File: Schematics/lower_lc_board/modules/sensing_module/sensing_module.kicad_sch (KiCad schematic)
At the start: 26 parts, among them J4 HALL-1, J5 HALL-2, Q3 2N7002, U11 SI2301CDS-T1-GE3, U9 ADC_ADS131M04IPWR

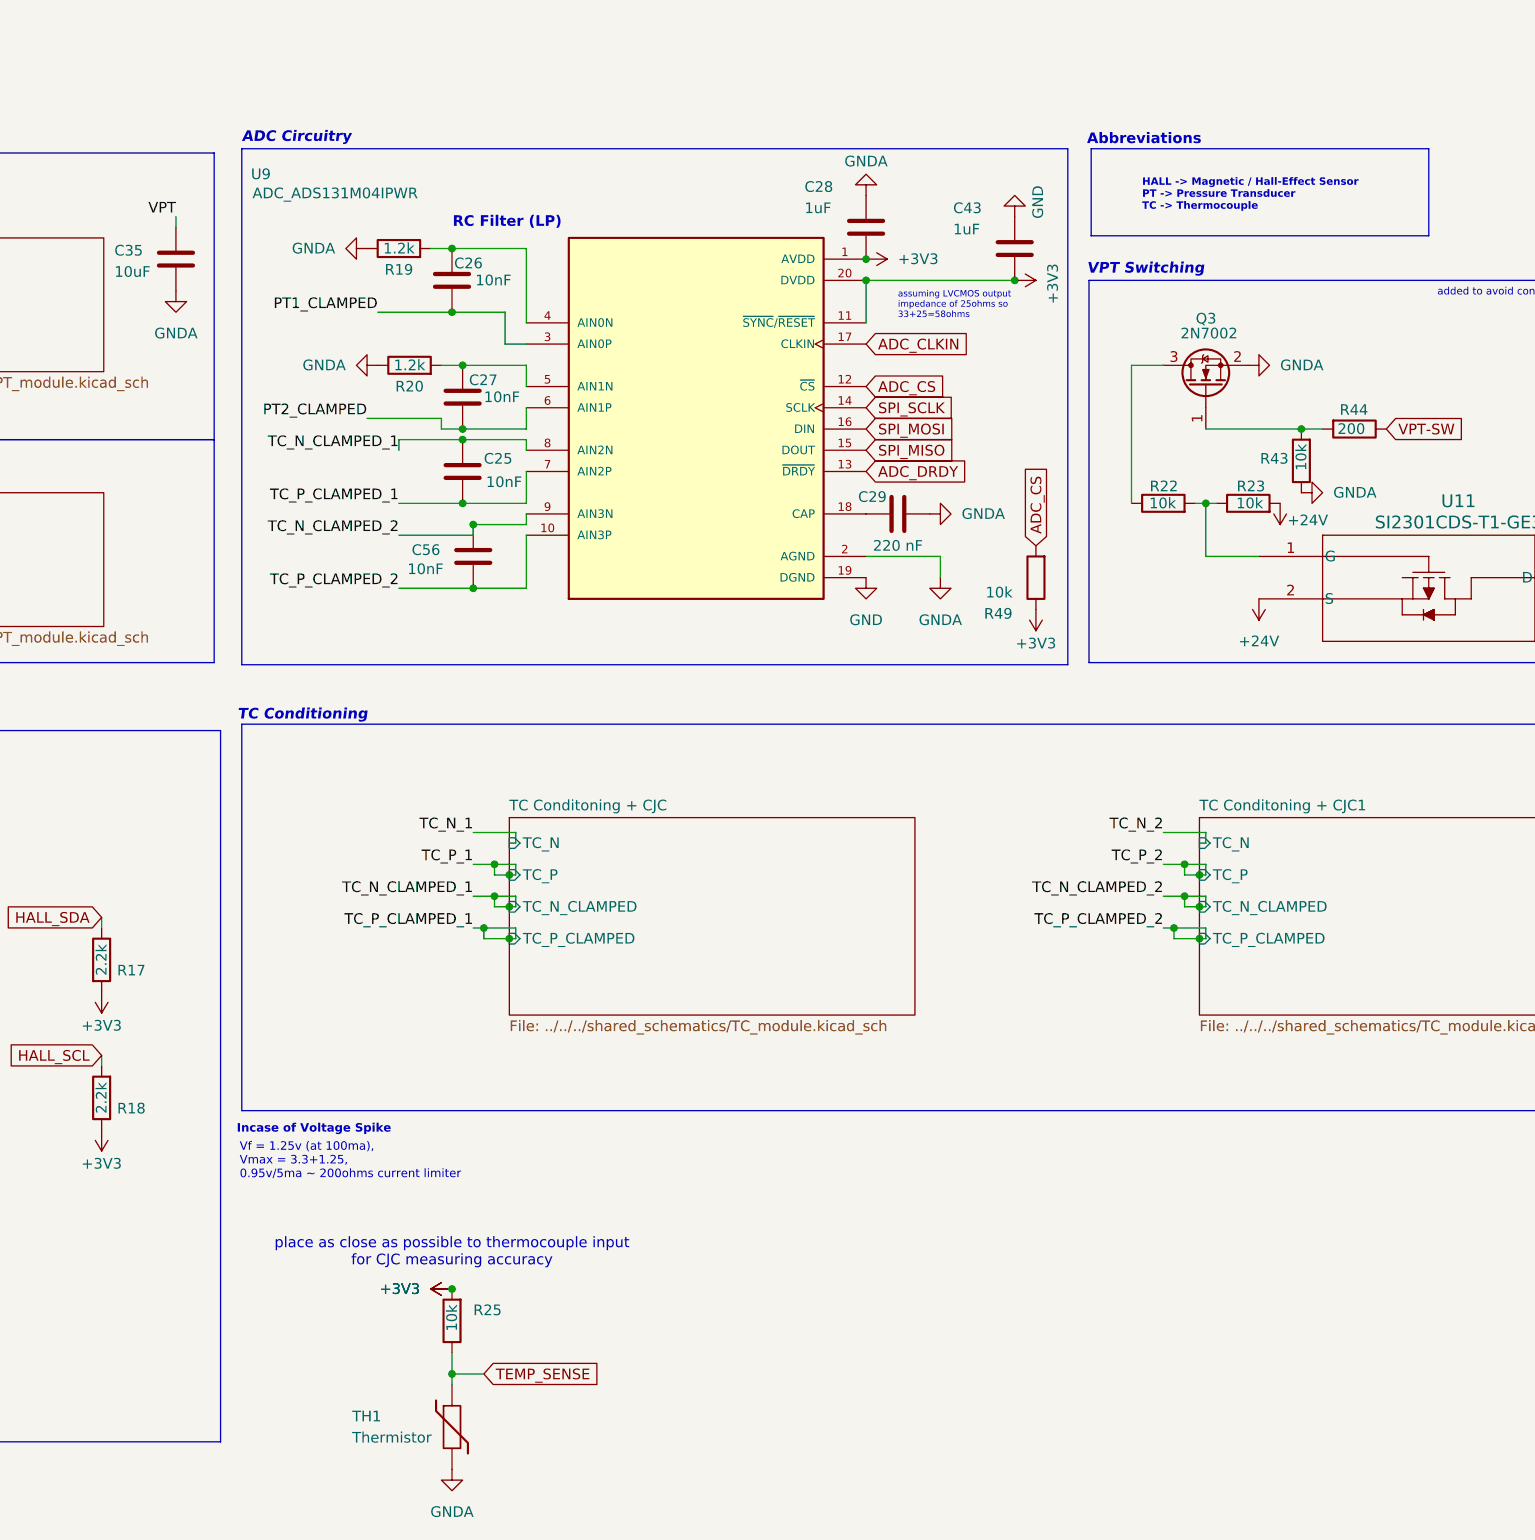
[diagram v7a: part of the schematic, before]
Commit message: remove AGND
simplicity
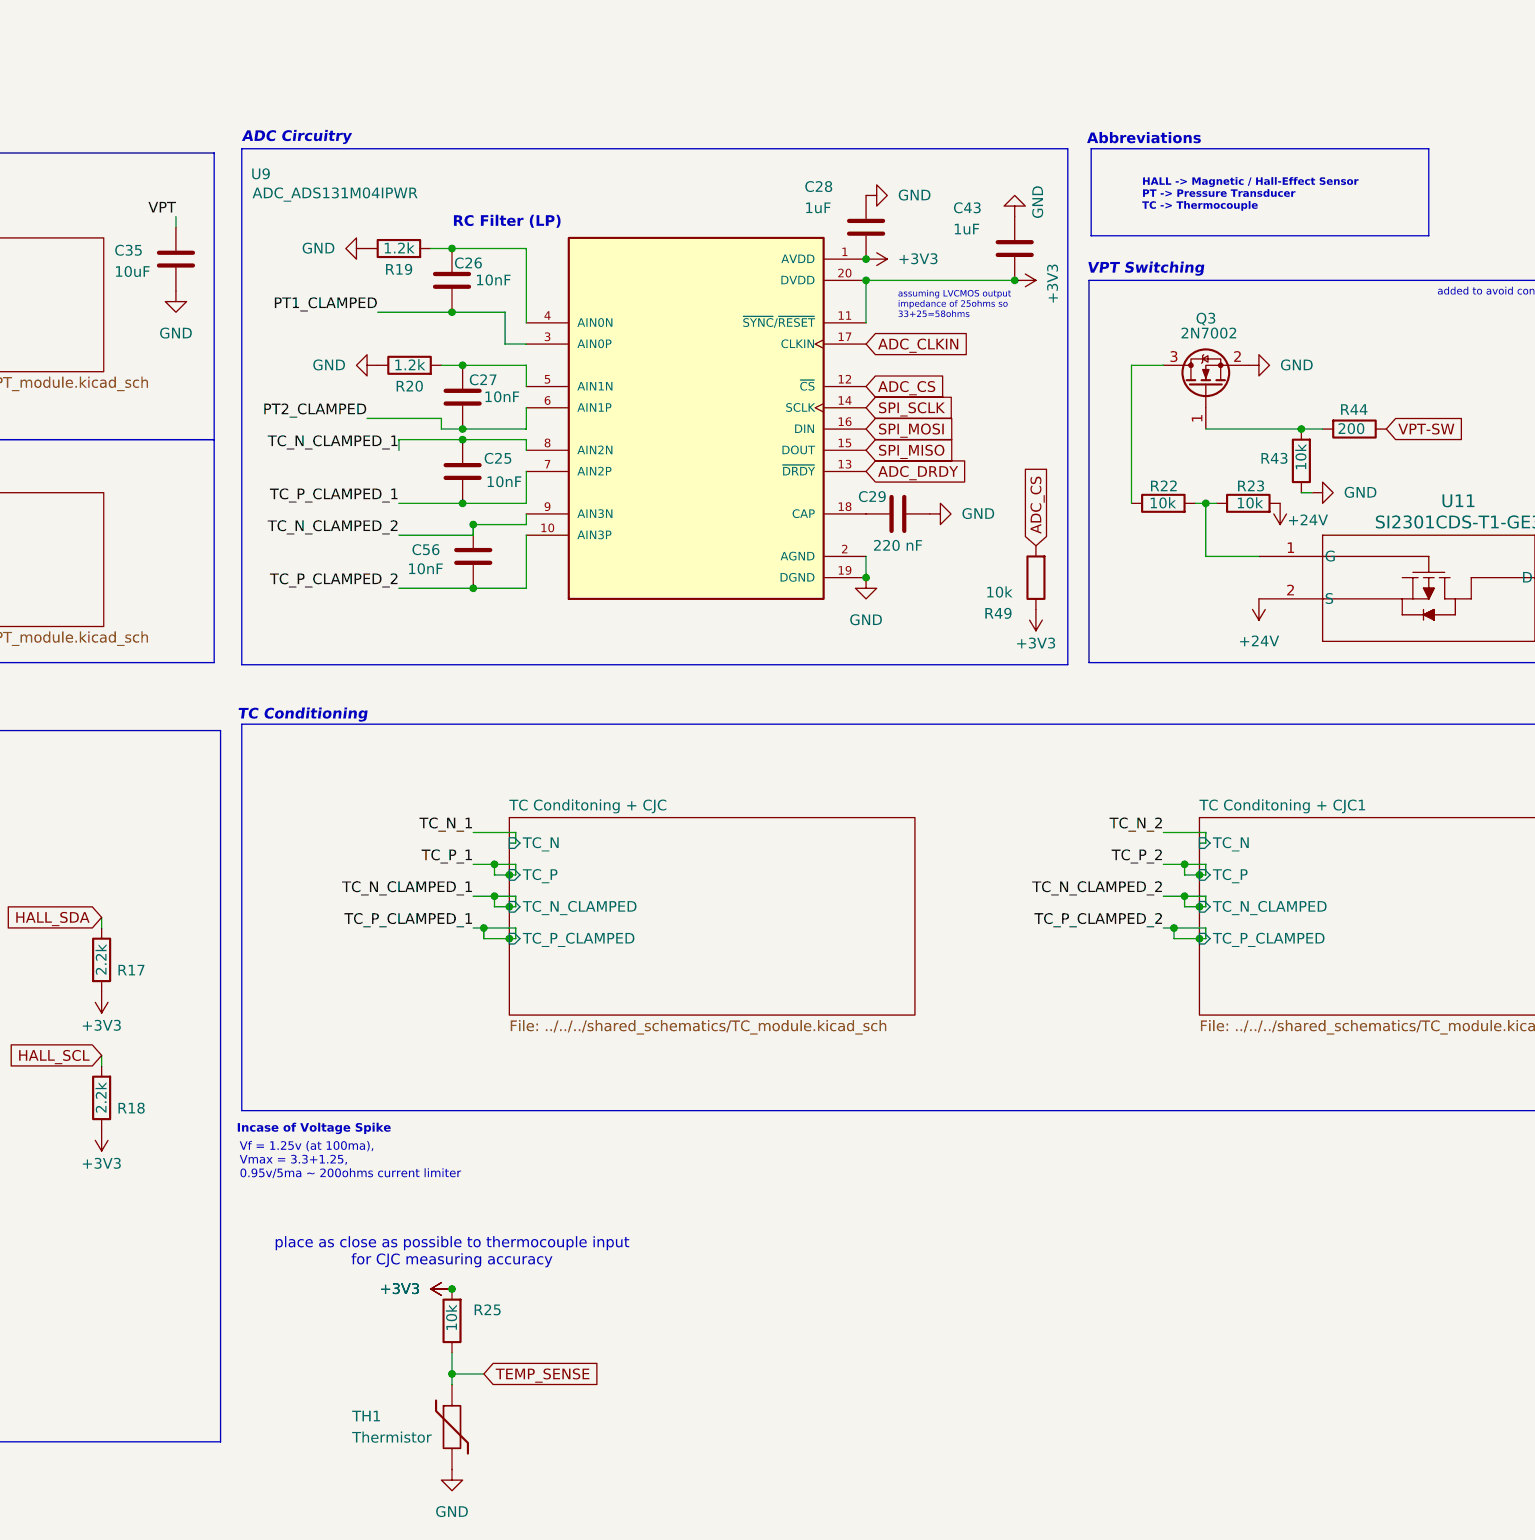
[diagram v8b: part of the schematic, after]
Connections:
- net GNDA is gone; now on net GND: C28.1, C29.2, C35.2, Q3.2 (S), R19.1, R20.1, R43.1, TH1.2, U9.2 (AGND)
